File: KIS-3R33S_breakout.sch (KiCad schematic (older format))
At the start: 7 parts, among them P1 Screw terminal, P2 Screw terminal, U1 KIS-3R33S_modif

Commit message: Throwing parts around.
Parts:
- C1: footprint (none) -> Capacitors:c_elec_SMD_12.5x13.5
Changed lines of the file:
@@
 F 0 "C1" H 5160 3820 50  0000 L CNN
 F 1 "1mF, 25V" H 5250 3750 50  0000 L CNN
-F 2 "" H 5150 3750 60  0001 C CNN
+F 2 "Capacitors:c_elec_SMD_12.5x13.5" H 5150 3750 60  0001 C CNN
 F 3 "" H 5150 3750 60  0000 C CNN
 	1    5150 3750

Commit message: Done?
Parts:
- RV1: footprint (none) -> Potentiometers:trimmer-pot_side-adjust_TSR-3006P_TH
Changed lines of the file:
@@
 F 0 "RV1" H 5900 3500 50  0000 C CNN
 F 1 "100k" H 5900 3600 50  0000 C CNN
-F 2 "" H 5900 3600 60  0001 C CNN
+F 2 "Potentiometers:trimmer-pot_side-adjust_TSR-3006P_TH" H 5900 3600 60  0001 C CNN
 F 3 "" H 5900 3600 60  0000 C CNN
 	1    5900 3600

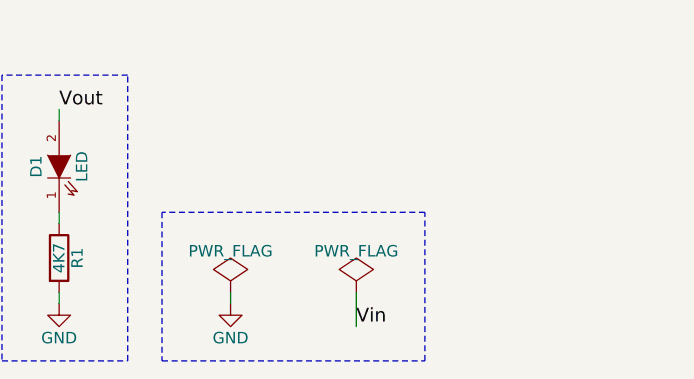
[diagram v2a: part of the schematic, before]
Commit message: Added optional descrete resistive-divider.
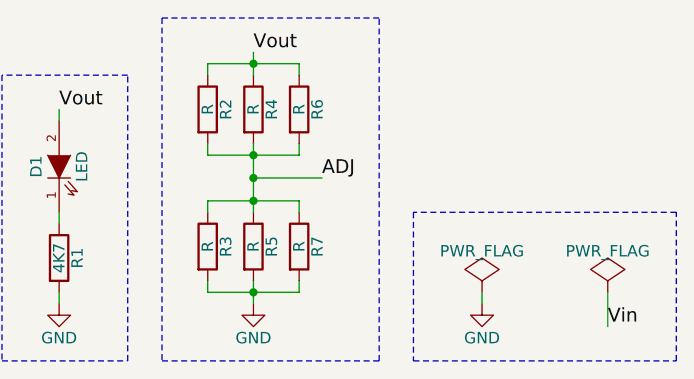
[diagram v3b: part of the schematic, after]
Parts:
- added R2, R3, R4, R5, R6, R7: R, Resistors_SMD:R_0603_HandSoldering, symbol R
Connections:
- net ADJ: now also R2.2, R3.1, R4.2, R5.1, R6.2, R7.1
- net GND: now also R3.2, R5.2, R7.2
- net Vout: now also R2.1, R4.1, R6.1
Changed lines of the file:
@@
 Sheet 1 1
 Title "KIS-3R33S_breakout"
-Date "Sat 02 May 2015"
-Rev "0.10"
+Date "Sun 03 May 2015"
+Rev "0.11"
 Comp "2015 - blog.spitzenpfeil.org"
 Comment1 ""
@@
 L PWR_FLAG #FLG03
 U 1 1 55452010
-P 8000 4000
-F 0 "#FLG03" H 8000 4095 50  0001 C CNN
-F 1 "PWR_FLAG" H 8000 4180 50  0000 C CNN
-F 2 "" H 8000 4000 60  0000 C CNN
-F 3 "" H 8000 4000 60  0000 C CNN
-	1    8000 4000
+P 9100 4000
+F 0 "#FLG03" H 9100 4095 50  0001 C CNN
+F 1 "PWR_FLAG" H 9100 4180 50  0000 C CNN
+F 2 "" H 9100 4000 60  0000 C CNN
+F 3 "" H 9100 4000 60  0000 C CNN
+	1    9100 4000
 	1    0    0    -1
 $EndComp
@@
 L GND #PWR04
 U 1 1 55452029
-P 8000 4050
-F 0 "#PWR04" H 8000 3800 50  0001 C CNN
-F 1 "GND" H 8000 3900 50  0000 C CNN
-F 2 "" H 8000 4050 60  0000 C CNN
-F 3 "" H 8000 4050 60  0000 C CNN
-	1    8000 4050
-	1    0    0    -1
-$EndComp
-Wire Wire Line
-	8000 4000 8000 4050
+P 9100 4050
+F 0 "#PWR04" H 9100 3800 50  0001 C CNN
+F 1 "GND" H 9100 3900 50  0000 C CNN
+F 2 "" H 9100 4050 60  0000 C CNN
+F 3 "" H 9100 4050 60  0000 C CNN
+	1    9100 4050
+	1    0    0    -1
+$EndComp
+Wire Wire Line
+	9100 4000 9100 4050
 $Comp
 L PWR_FLAG #FLG05
 U 1 1 55452080
-P 8550 4000
-F 0 "#FLG05" H 8550 4095 50  0001 C CNN
-F 1 "PWR_FLAG" H 8550 4180 50  0000 C CNN
-F 2 "" H 8550 4000 60  0000 C CNN
-F 3 "" H 8550 4000 60  0000 C CNN
-	1    8550 4000
-	1    0    0    -1
-$EndComp
-Text Label 8550 4150 0    60   ~ 0
+P 9650 4000
+F 0 "#FLG05" H 9650 4095 50  0001 C CNN
+F 1 "PWR_FLAG" H 9650 4180 50  0000 C CNN
+F 2 "" H 9650 4000 60  0000 C CNN
+F 3 "" H 9650 4000 60  0000 C CNN
+	1    9650 4000
+	1    0    0    -1
+$EndComp
+Text Label 9650 4150 0    60   ~ 0
 Vin
 Wire Wire Line
-	8550 4000 8550 4150
+	9650 4000 9650 4150
 Text Label 3800 3700 0    60   ~ 0
 Vin
 Wire Notes Line
-	7700 3650 7700 4300
-Wire Notes Line
-	7700 4300 8850 4300
-Wire Notes Line
-	8850 4300 8850 3650
-Wire Notes Line
-	8850 3650 7700 3650
+	8800 3650 8800 4300
+Wire Notes Line
+	8800 4300 9950 4300
+Wire Notes Line
+	9950 4300 9950 3650
+Wire Notes Line
+	9950 3650 8800 3650
 Wire Notes Line
 	2950 3050 2950 4300
@@
 Wire Notes Line
 	7550 3050 7000 3050
+$Comp
+L R R2
+U 1 1 5545EA77
+P 7900 3200
+F 0 "R2" V 7980 3200 50  0000 C CNN
+F 1 "R" V 7900 3200 50  0000 C CNN
+F 2 "Resistors_SMD:R_0603_HandSoldering" V 7830 3200 30  0001 C CNN
+F 3 "" H 7900 3200 30  0000 C CNN
+	1    7900 3200
+	1    0    0    -1
+$EndComp
+$Comp
+L R R4
+U 1 1 5545EADA
+P 8100 3200
+F 0 "R4" V 8180 3200 50  0000 C CNN
+F 1 "R" V 8100 3200 50  0000 C CNN
+F 2 "Resistors_SMD:R_0603_HandSoldering" V 8030 3200 30  0001 C CNN
+F 3 "" H 8100 3200 30  0000 C CNN
+	1    8100 3200
+	1    0    0    -1
+$EndComp
+$Comp
+L R R6
+U 1 1 5545EB02
+P 8300 3200
+F 0 "R6" V 8380 3200 50  0000 C CNN
+F 1 "R" V 8300 3200 50  0000 C CNN
+F 2 "Resistors_SMD:R_0603_HandSoldering" V 8230 3200 30  0001 C CNN
+F 3 "" H 8300 3200 30  0000 C CNN
+	1    8300 3200
+	1    0    0    -1
+$EndComp
+$Comp
+L R R3
+U 1 1 5545EB2F
+P 7900 3800
+F 0 "R3" V 7980 3800 50  0000 C CNN
+F 1 "R" V 7900 3800 50  0000 C CNN
+F 2 "Resistors_SMD:R_0603_HandSoldering" V 7830 3800 30  0001 C CNN
+F 3 "" H 7900 3800 30  0000 C CNN
+	1    7900 3800
+	1    0    0    -1
+$EndComp
+$Comp
+L R R5
+U 1 1 5545EB5D
+P 8100 3800
+F 0 "R5" V 8180 3800 50  0000 C CNN
+F 1 "R" V 8100 3800 50  0000 C CNN
+F 2 "Resistors_SMD:R_0603_HandSoldering" V 8030 3800 30  0001 C CNN
+F 3 "" H 8100 3800 30  0000 C CNN
+	1    8100 3800
+	1    0    0    -1
+$EndComp
+$Comp
+L R R7
+U 1 1 5545EB90
+P 8300 3800
+F 0 "R7" V 8380 3800 50  0000 C CNN
+F 1 "R" V 8300 3800 50  0000 C CNN
+F 2 "Resistors_SMD:R_0603_HandSoldering" V 8230 3800 30  0001 C CNN
+F 3 "" H 8300 3800 30  0000 C CNN
+	1    8300 3800
+	1    0    0    -1
+$EndComp
+$Comp
+L GND #PWR07
+U 1 1 5545EE5C
+P 8100 4050
+F 0 "#PWR07" H 8100 3800 50  0001 C CNN
+F 1 "GND" H 8100 3900 50  0000 C CNN
+F 2 "" H 8100 4050 60  0000 C CNN
+F 3 "" H 8100 4050 60  0000 C CNN
+	1    8100 4050
+	1    0    0    -1
+$EndComp
+Text Label 8100 2950 0    60   ~ 0
+Vout
+Wire Wire Line
+	7900 3950 7900 4000
+Wire Wire Line
+	8300 4000 8300 3950
+Wire Wire Line
+	8100 3950 8100 4050
+Wire Wire Line
+	7900 4000 8300 4000
+Connection ~ 8100 4000
+Wire Wire Line
+	7900 3050 7900 3000
+Wire Wire Line
+	7900 3000 8300 3000
+Wire Wire Line
+	8300 3000 8300 3050
+Wire Wire Line
+	8100 2950 8100 3050
+Connection ~ 8100 3000
+Wire Wire Line
+	7900 3350 7900 3400
+Wire Wire Line
+	7900 3400 8300 3400
+Wire Wire Line
+	8300 3400 8300 3350
+Wire Wire Line
+	8100 3350 8100 3650
+Connection ~ 8100 3400
+Wire Wire Line
+	7900 3650 7900 3600
+Wire Wire Line
+	7900 3600 8300 3600
+Wire Wire Line
+	8300 3600 8300 3650
+Connection ~ 8100 3600
+Text Label 8400 3500 0    60   ~ 0
+ADJ
+Wire Wire Line
+	8100 3500 8400 3500
+Connection ~ 8100 3500
+Wire Notes Line
+	7700 2800 7700 4300
+Wire Notes Line
+	7700 4300 8650 4300
+Wire Notes Line
+	8650 4300 8650 2800
+Wire Notes Line
+	8650 2800 7700 2800
 $EndSCHEMATC

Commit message: Adjustment pot was reversed. Vout should go up turning clockwise.
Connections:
- net GND: now also RV1.3; no longer RV1.1
- net Vout: now also RV1.1; no longer RV1.3
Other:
- note added: "Trimmer 20-turn\n(clockwise: 2-->3)"
- note removed: "Trimmer 20-turn"
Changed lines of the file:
@@
 Title "KIS-3R33S_breakout"
 Date "Sun 03 May 2015"
-Rev "0.11"
+Rev "0.12"
 Comp "2015 - blog.spitzenpfeil.org"
 Comment1 ""
@@
 F 3 "" H 5900 3600 60  0000 C CNN
 	1    5900 3600
-	0    -1   -1   0
+	0    -1   1    0
 $EndComp
 Connection ~ 5150 3850
@@
 $EndComp
 Text Notes 5700 4000 0    39   ~ 0
-Trimmer 20-turn
+Trimmer 20-turn\n(clockwise: 2-->3)
 Text Label 5650 3600 2    60   ~ 0
 ADJ

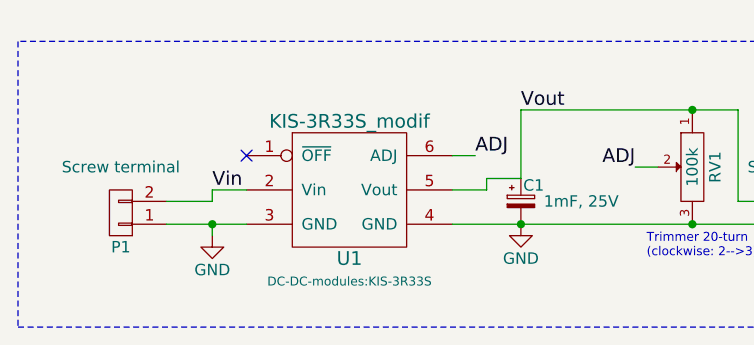
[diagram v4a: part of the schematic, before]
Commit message: Added comment to schematic.
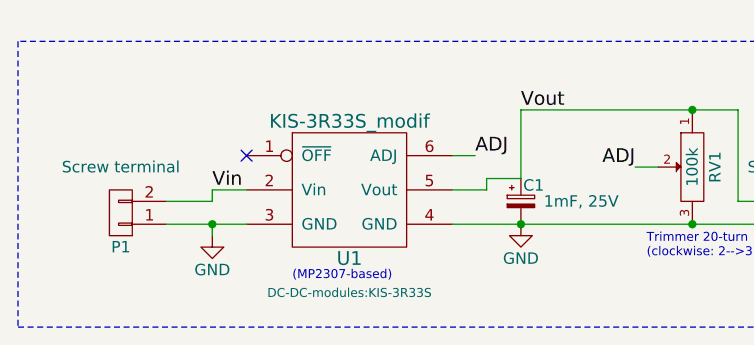
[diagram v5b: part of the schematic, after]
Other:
- note added: "(MP2307-based)"
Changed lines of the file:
@@
 F 0 "U1" H 4400 3400 60  0000 C CNN
 F 1 "KIS-3R33S_modif" H 4400 4000 60  0000 C CNN
-F 2 "DC-DC-modules:KIS-3R33S" H 4400 3300 39  0000 C CNN
+F 2 "DC-DC-modules:KIS-3R33S" H 4400 3250 39  0000 C CNN
 F 3 "" H 4150 3650 60  0000 C CNN
 	1    4400 3700
@@
 Wire Notes Line
 	8650 2800 7700 2800
+Text Notes 4150 4100 0    39   ~ 0
+(MP2307-based)
 $EndSCHEMATC
